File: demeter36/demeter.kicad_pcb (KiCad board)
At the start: 2 copper layers, 116.2 x 107.4 mm, 24 parts, among them SW10 SW_Push, SW11 SW_Push, SW12 SW_Push, SW14 SW_Push, SW15 SW_Push, SW16 SW_Push, SW17 SW_Push, SW18 SW_Push, SW2 SW_Push, SW2 SW_SPDT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

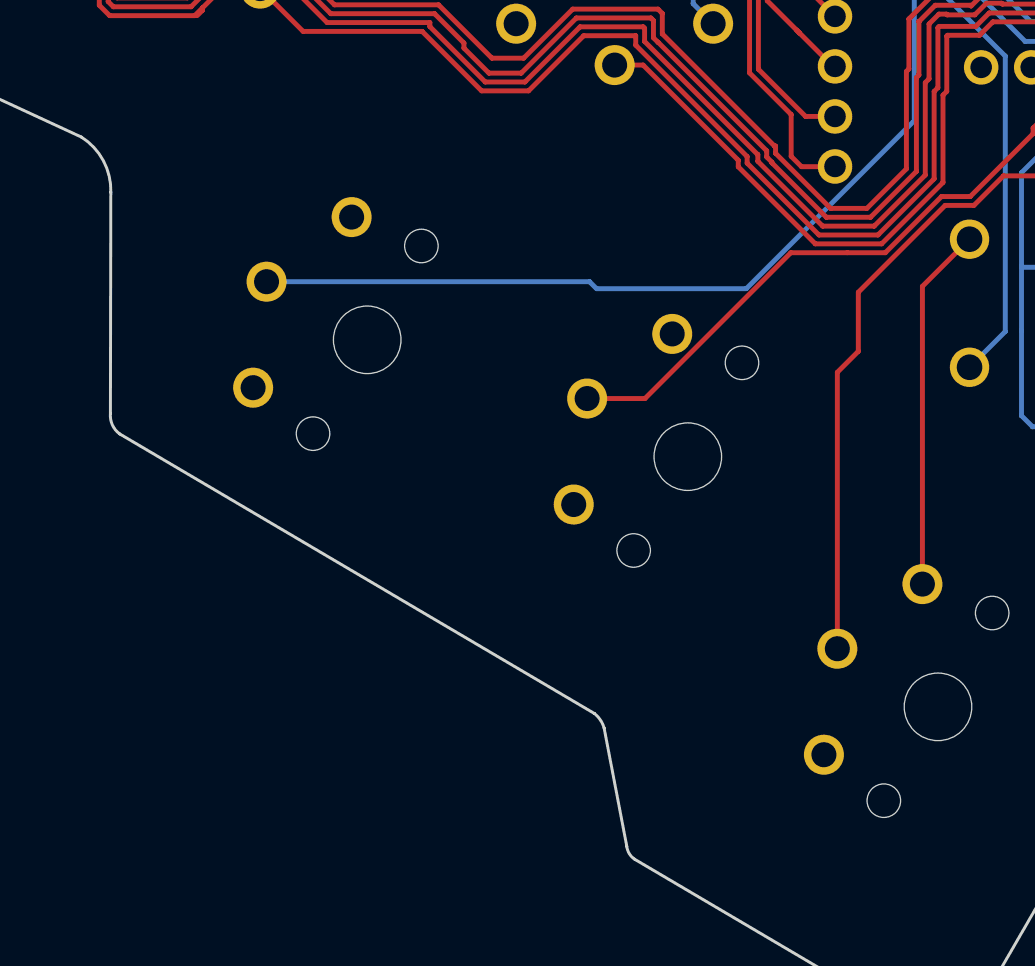
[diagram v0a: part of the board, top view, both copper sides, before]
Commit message: move third thumb a bit
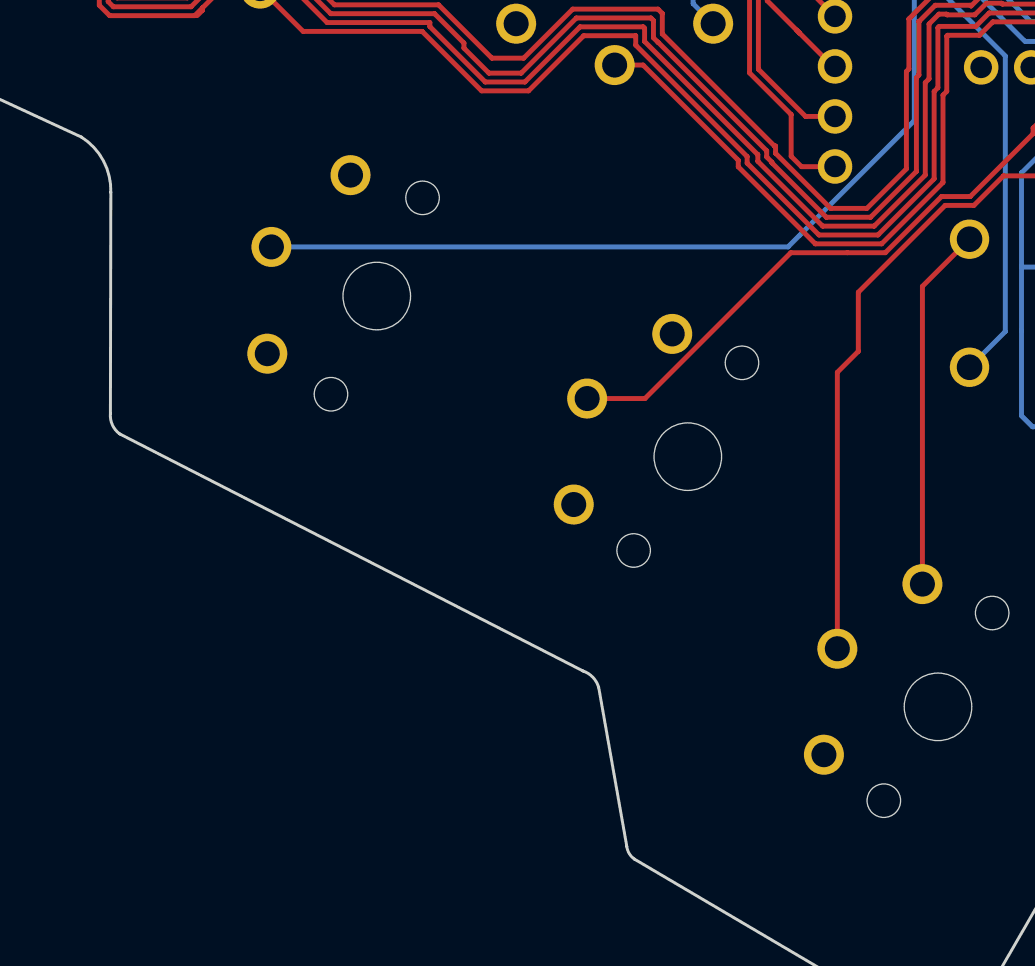
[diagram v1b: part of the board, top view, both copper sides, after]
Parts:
- moved SW20 2.27 mm to (145.8, 114.5), turned to -115 degrees
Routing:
- net Switch18: track 70.6 -> 69.3 mm
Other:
- outline, holes or cut-outs redrawn
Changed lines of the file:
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@@
   )
   (footprint "Kailh:SW_PG1350_rev_DPB2.2" (layer "F.Cu")
-    (at 145.35 116.74686 -120)
+    (at 145.8344 114.525307 -115)
     (descr "Kailh \"Choc\" PG1350 keyswitch, able to be mounted on front or back of PCB")
     (tags "kailh,choc")
@@
     (property "Sheetname" "")
     (attr through_hole)
-    (fp_text reference "SW20" (at 4.98 -5.69 60) (layer "Dwgs.User") hide
+    (fp_text reference "SW20" (at 4.98 -5.69 65) (layer "Dwgs.User") hide
         (effects (font (size 1 1) (thickness 0.15)))
     )
-    (fp_text value "SW_Push" (at -0.07 8.17 60) (layer "Dwgs.User") hide
+    (fp_text value "SW_Push" (at -0.07 8.17 65) (layer "Dwgs.User") hide
         (effects (font (size 1 1) (thickness 0.15)))
     )
-    (fp_text user "${REFERENCE}" (at 0.06 0.06 60) (layer "B.SilkS")
-        (effects (font (size 1 1) (thickness 0.15)) (justify mirror))
-    )
-    (fp_text user "CPG1232 - 12.7x13.7 plate cutout" (at 0 -7.7 60) (layer "Cmts.User")
+    (fp_text user "${REFERENCE}" (at 0.06 0.06 65) (layer "B.SilkS")
+        (effects (font (size 1 1) (thickness 0.15)) (justify mirror))
+    )
+    (fp_text user "CPG1232 - 12.7x13.7 plate cutout" (at 0 -7.7 65) (layer "Cmts.User")
         (effects (font (size 1 1) (thickness 0.15)))
     )
-    (fp_text user "${VALUE}" (at 0 8.255 60) (layer "B.Fab")
-        (effects (font (size 1 1) (thickness 0.15)) (justify mirror))
-    )
-    (fp_text user "${REFERENCE}" (at 0 0 60) (layer "F.Fab")
+    (fp_text user "${VALUE}" (at 0 8.255 65) (layer "B.Fab")
+        (effects (font (size 1 1) (thickness 0.15)) (justify mirror))
+    )
+    (fp_text user "${REFERENCE}" (at 0 0 65) (layer "F.Fab")
         (effects (font (size 1 1) (thickness 0.15)))
     )
@@
     (fp_line (start 7.5 7.5) (end -7.5 7.5)
       (stroke (width 0.15) (type solid)) (layer "F.Fab"))
-    (pad "" np_thru_hole circle (at -5.5 0 240) (size 1.7018 1.7018) (drill 1.7018) (layers "*.Cu" "*.Mask"))
-    (pad "" np_thru_hole circle (at 0 0 240) (size 3.429 3.429) (drill 3.429) (layers "*.Cu" "*.Mask"))
-    (pad "" np_thru_hole circle (at 5.5 0 240) (size 1.7018 1.7018) (drill 1.7018) (layers "*.Cu" "*.Mask"))
-    (pad "1" thru_hole circle (at 0 5.9 240) (size 2.032 2.032) (drill 1.27) (layers "*.Cu" "*.Mask")
+    (pad "" np_thru_hole circle (at -5.5 0 245) (size 1.7018 1.7018) (drill 1.7018) (layers "*.Cu" "*.Mask"))
+    (pad "" np_thru_hole circle (at 0 0 245) (size 3.429 3.429) (drill 3.429) (layers "*.Cu" "*.Mask"))
+    (pad "" np_thru_hole circle (at 5.5 0 245) (size 1.7018 1.7018) (drill 1.7018) (layers "*.Cu" "*.Mask"))
+    (pad "1" thru_hole circle (at 0 5.9 245) (size 2.032 2.032) (drill 1.27) (layers "*.Cu" "*.Mask")
       (net 4 "Switch18") (pinfunction "1") (pintype "passive"))
-    (pad "2" thru_hole circle (at -5 3.8 240) (size 2.032 2.032) (drill 1.27) (layers "*.Cu" "*.Mask")
+    (pad "2" thru_hole circle (at -5 3.8 245) (size 2.032 2.032) (drill 1.27) (layers "*.Cu" "*.Mask")
       (net 2 "gnd") (pinfunction "2") (pintype "passive"))
-    (pad "2" thru_hole circle (at 5 3.8 240) (size 2.032 2.032) (drill 1.27) (layers "*.Cu" "*.Mask")
+    (pad "2" thru_hole circle (at 5 3.8 245) (size 2.032 2.032) (drill 1.27) (layers "*.Cu" "*.Mask")
       (net 2 "gnd") (pinfunction "2") (pintype "passive"))
   )
@@
   (gr_arc (start 185.868101 121.827278) (mid 185.42487 118.778881) (end 185.911057 115.737038)
     (stroke (width 0.15) (type solid)) (layer "Edge.Cuts"))
-  (gr_line (start 132.784652 121.52306) (end 156.89 135.72)
+  (gr_line (start 132.784652 121.52306) (end 156.31 133.56)
     (stroke (width 0.15) (type solid)) (layer "Edge.Cuts"))
   (gr_line (start 112.656447 49.806447) (end 112.614589 45.671567)
@@
   (gr_arc (start 130.845241 106.456764) (mid 131.96 107.66) (end 132.335241 109.256764)
     (stroke (width 0.15) (type default)) (layer "Edge.Cuts"))
-  (gr_arc (start 156.89 135.72) (mid 157.187676 136.046512) (end 157.374342 136.446985)
+  (gr_arc (start 156.31 133.56) (mid 156.805688 133.879164) (end 157.1 134.39)
     (stroke (width 0.15) (type default)) (layer "Edge.Cuts"))
   (gr_arc (start 132.784652 121.52306) (mid 132.412883 121.064871) (end 132.314652 120.48306)
@@
   (gr_line (start 97.71 102.19) (end 120.5 102.16)
     (stroke (width 0.15) (type solid)) (layer "Edge.Cuts"))
-  (gr_line (start 157.374342 136.446985) (end 158.528624 142.469539)
+  (gr_line (start 157.1 134.39) (end 158.528624 142.469539)
     (stroke (width 0.15) (type solid)) (layer "Edge.Cuts"))
   (gr_line (start 131.064 49.764) (end 131.064 45.514)
@@
   (via (at 177.221918 83.566) (size 0.8) (drill 0.4) (layers "F.Cu" "B.Cu") (net 4))
   (via (at 173.120418 98.806) (size 0.8) (drill 0.4) (layers "F.Cu" "B.Cu") (net 4))
+  (segment (start 140.487184 112.031859) (end 166.710955 112.031859) (width 0.25) (layer "B.Cu") (net 4))
+  (segment (start 173.120418 105.622395) (end 167.306407 111.436407) (width 0.25) (layer "B.Cu") (net 4))
   (segment (start 176.967918 83.566) (end 176.840918 83.693) (width 0.25) (layer "B.Cu") (net 4))
   (segment (start 173.960918 83.693) (end 172.815918 82.548) (width 0.25) (layer "B.Cu") (net 4))
   (segment (start 173.120418 98.806) (end 173.120418 105.622395) (width 0.25) (layer "B.Cu") (net 4))
-  (segment (start 164.592813 114.15) (end 156.99 114.15) (width 0.25) (layer "B.Cu") (net 4))
   (segment (start 176.840918 83.693) (end 173.960918 83.693) (width 0.25) (layer "B.Cu") (net 4))
-  (segment (start 173.120418 105.622395) (end 164.592813 114.15) (width 0.25) (layer "B.Cu") (net 4))
   (segment (start 177.221918 83.566) (end 176.967918 83.566) (width 0.25) (layer "B.Cu") (net 4))
-  (segment (start 156.99 114.15) (end 156.63686 113.79686) (width 0.25) (layer "B.Cu") (net 4))
-  (segment (start 156.63686 113.79686) (end 140.24045 113.79686) (width 0.25) (layer "B.Cu") (net 4))
+  (segment (start 166.710955 112.031859) (end 167.306407 111.436407) (width 0.25) (layer "B.Cu") (net 4))
   (segment (start 171.45 95.179918) (end 174.300918 92.329) (width 0.25) (layer "F.Cu") (net 5))
   (segment (start 174.797918 91.832) (end 174.300918 92.329) (width 0.25) (layer "F.Cu") (net 5))
